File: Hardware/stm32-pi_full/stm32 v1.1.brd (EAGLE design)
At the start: 131.4 x 105.8 mm, 287 parts, among them IC2 AD8519KS, J1 JUMPER-SMT_2_NC_TRACE_NO-SILK, Q1 PNP, Q2 NPN, Q3 NPN, U1 ESP32-WROOM-32D

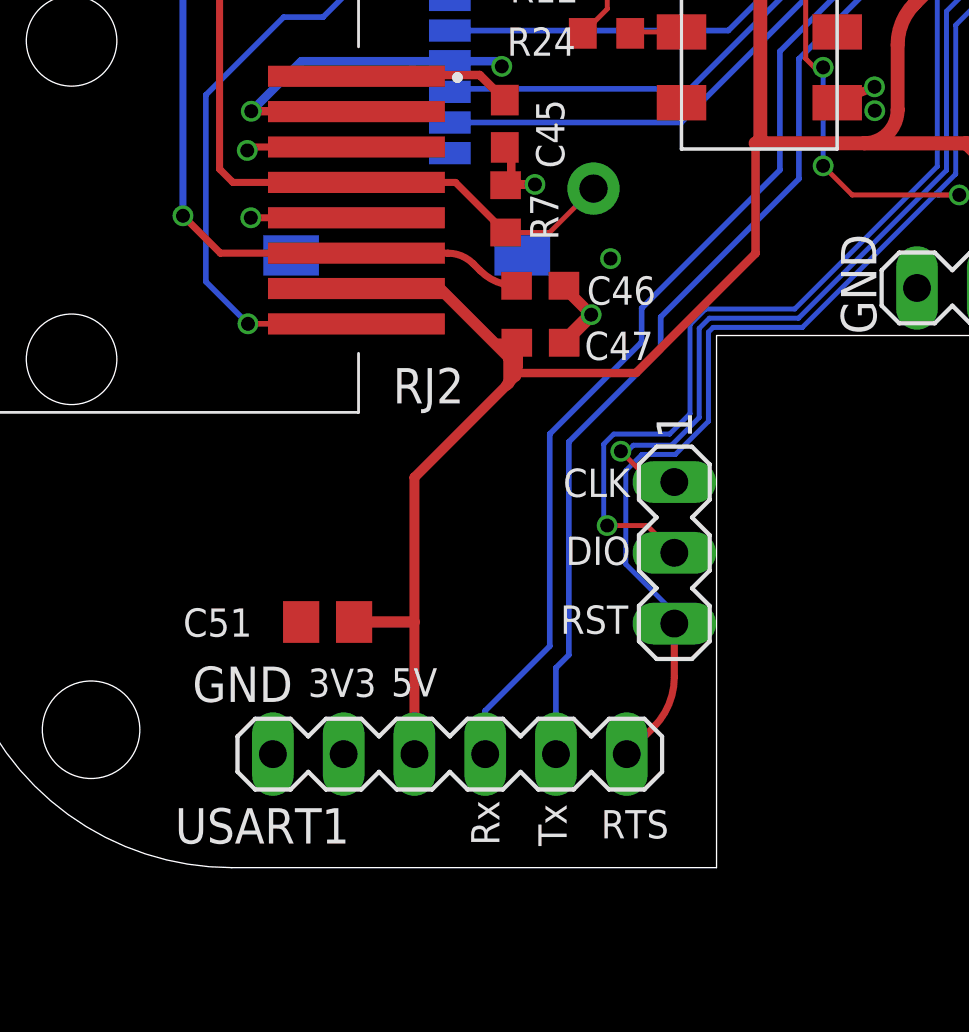
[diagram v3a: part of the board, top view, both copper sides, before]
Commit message: move UART header back away from case edge
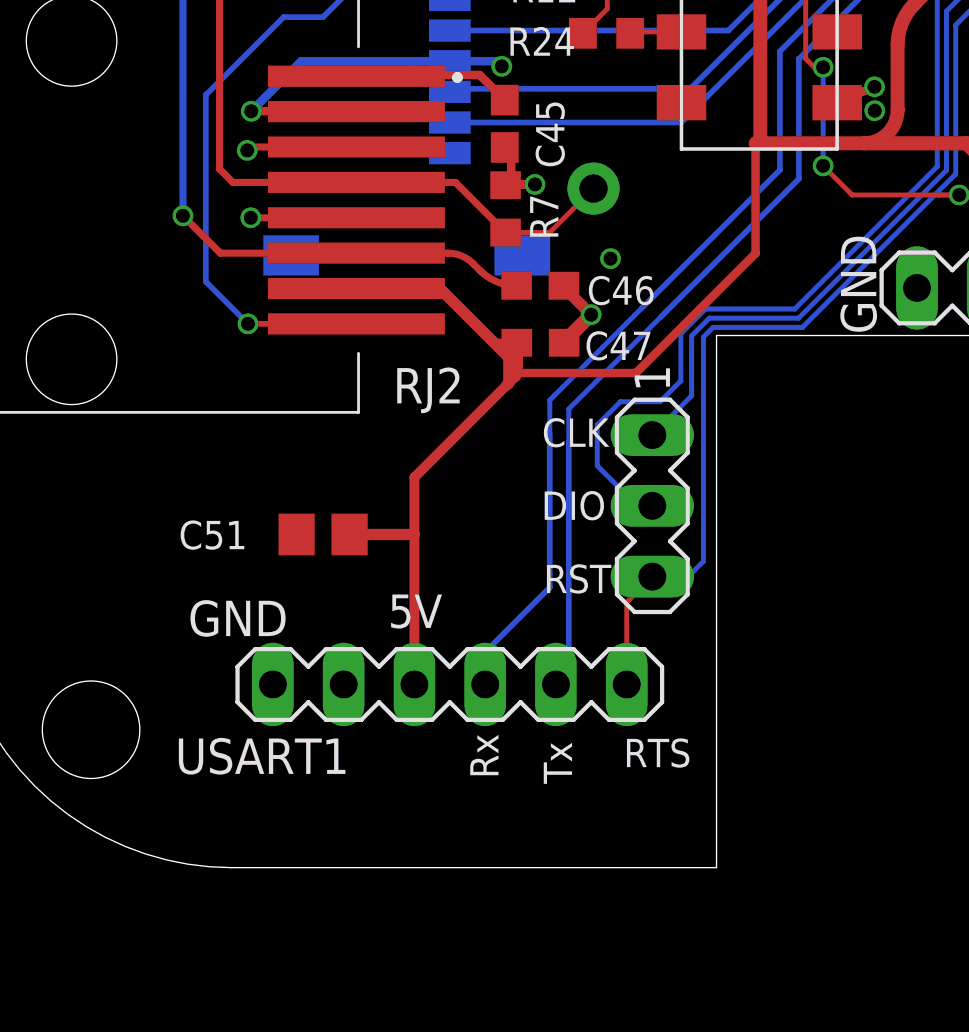
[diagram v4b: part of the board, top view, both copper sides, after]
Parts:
- moved C51 3.14 mm to (13.3, 12.0)
- moved USART1 2.50 mm to (17.8, 6.57)
- moved SV3 1.86 mm to (25.1, 13.0)
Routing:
- net SWCLK: track 59.2 -> 54.8 mm, vias 2 -> 1
- net NRST_STM: track 201.6 -> 197.8 mm
- net SWDIO: track 65.9 -> 63.3 mm, vias 2 -> 1
- net UART1_TX: track 107.0 -> 104.5 mm
- net UART1_RX: track 108.6 -> 106.1 mm
- net +5V: track 323.4 -> 321.1 mm
